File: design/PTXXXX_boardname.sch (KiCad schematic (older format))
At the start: 1 part

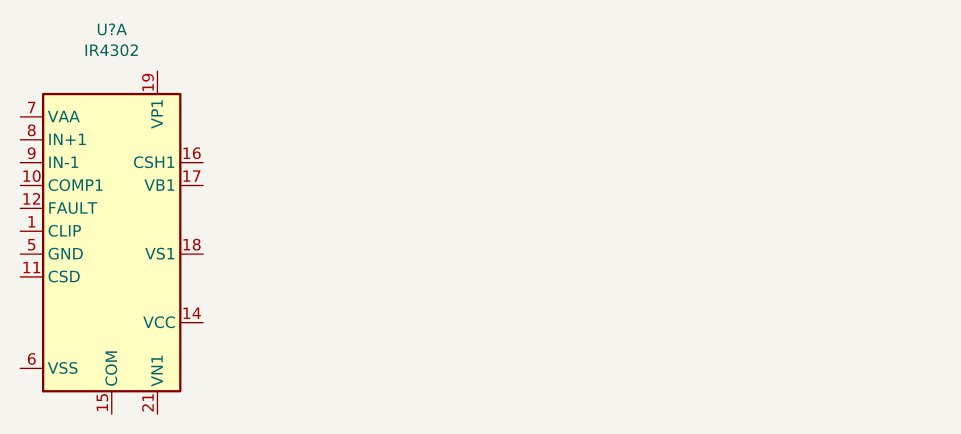
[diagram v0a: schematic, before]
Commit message: minor schematic change (text change to test, in reality would be something more important like DNF or value change) done in develop/1.0_1B branch
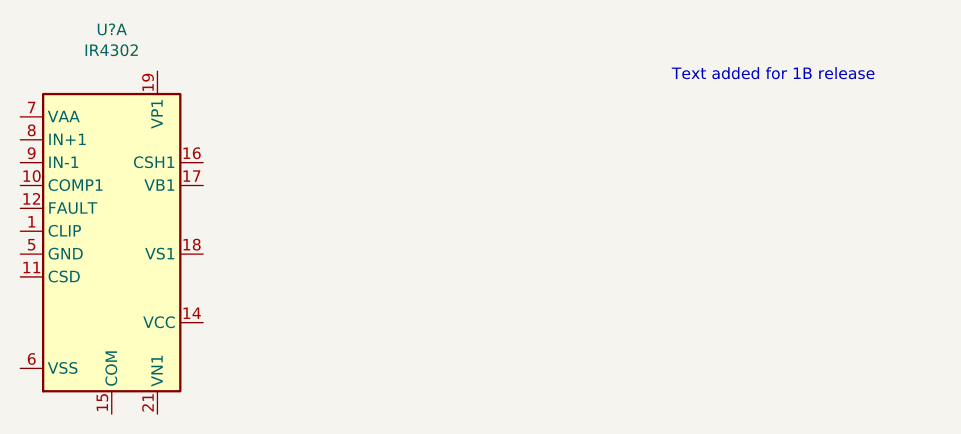
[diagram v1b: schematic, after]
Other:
- note added: "Text added for 1B release"
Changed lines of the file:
@@
 	1    0    0    -1
 $EndComp
+Text Notes 7100 2500 0    50   ~ 0
+Text added for 1B release
 $EndSCHEMATC
